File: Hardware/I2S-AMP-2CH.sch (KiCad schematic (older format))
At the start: 19 parts, among them U6 TAS5760MDCAR

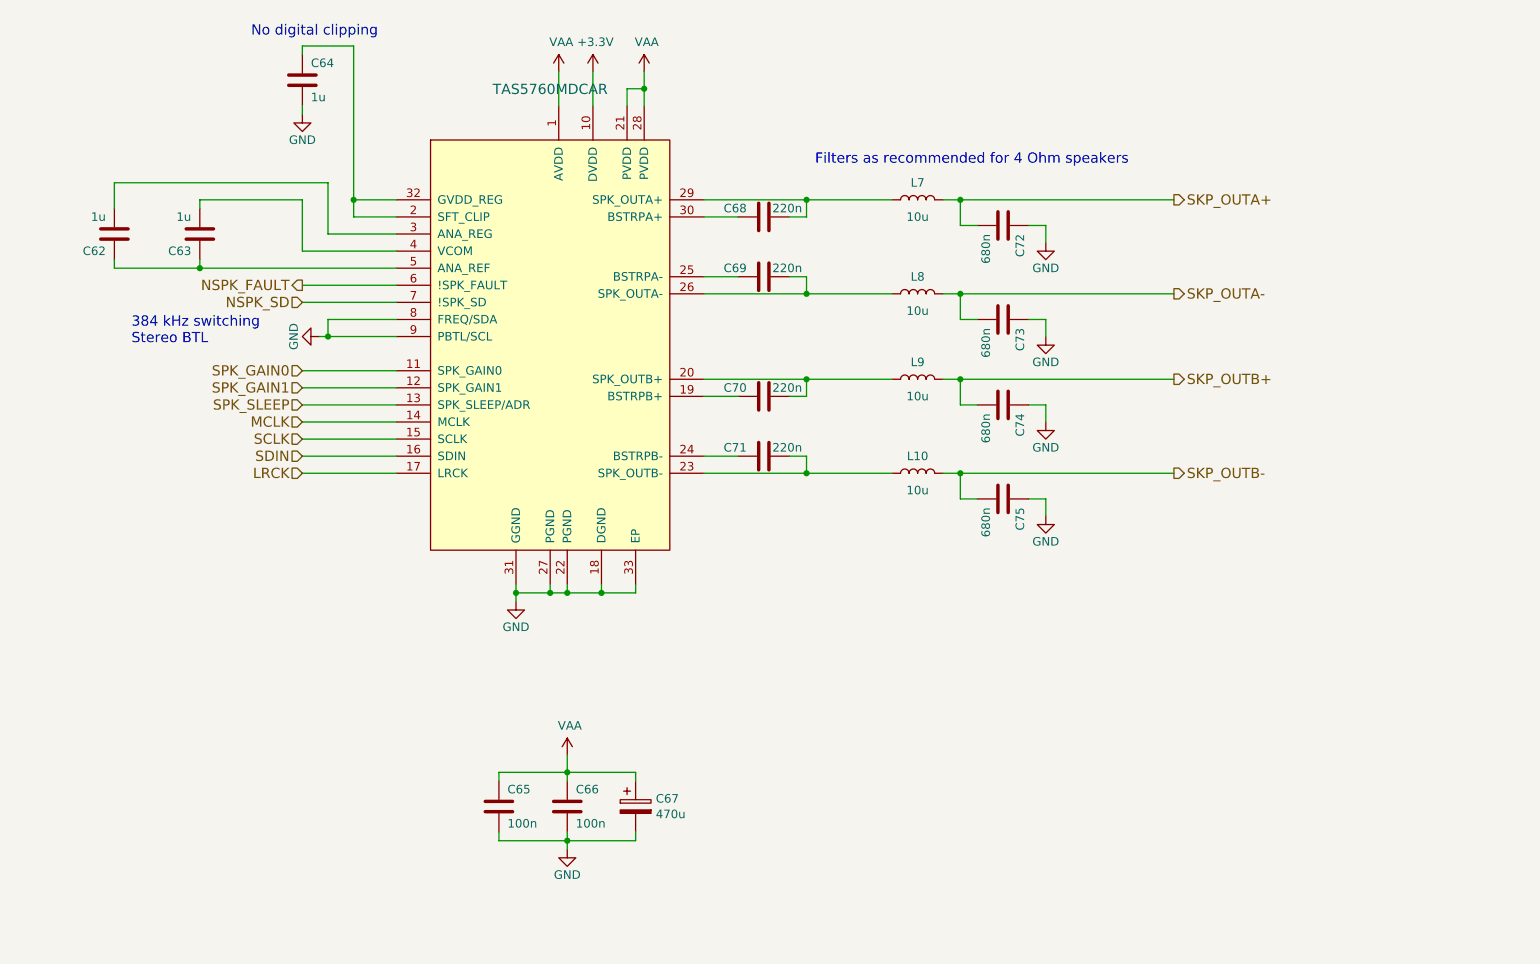
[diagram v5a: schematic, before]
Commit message: fixed usbi/ext header positions
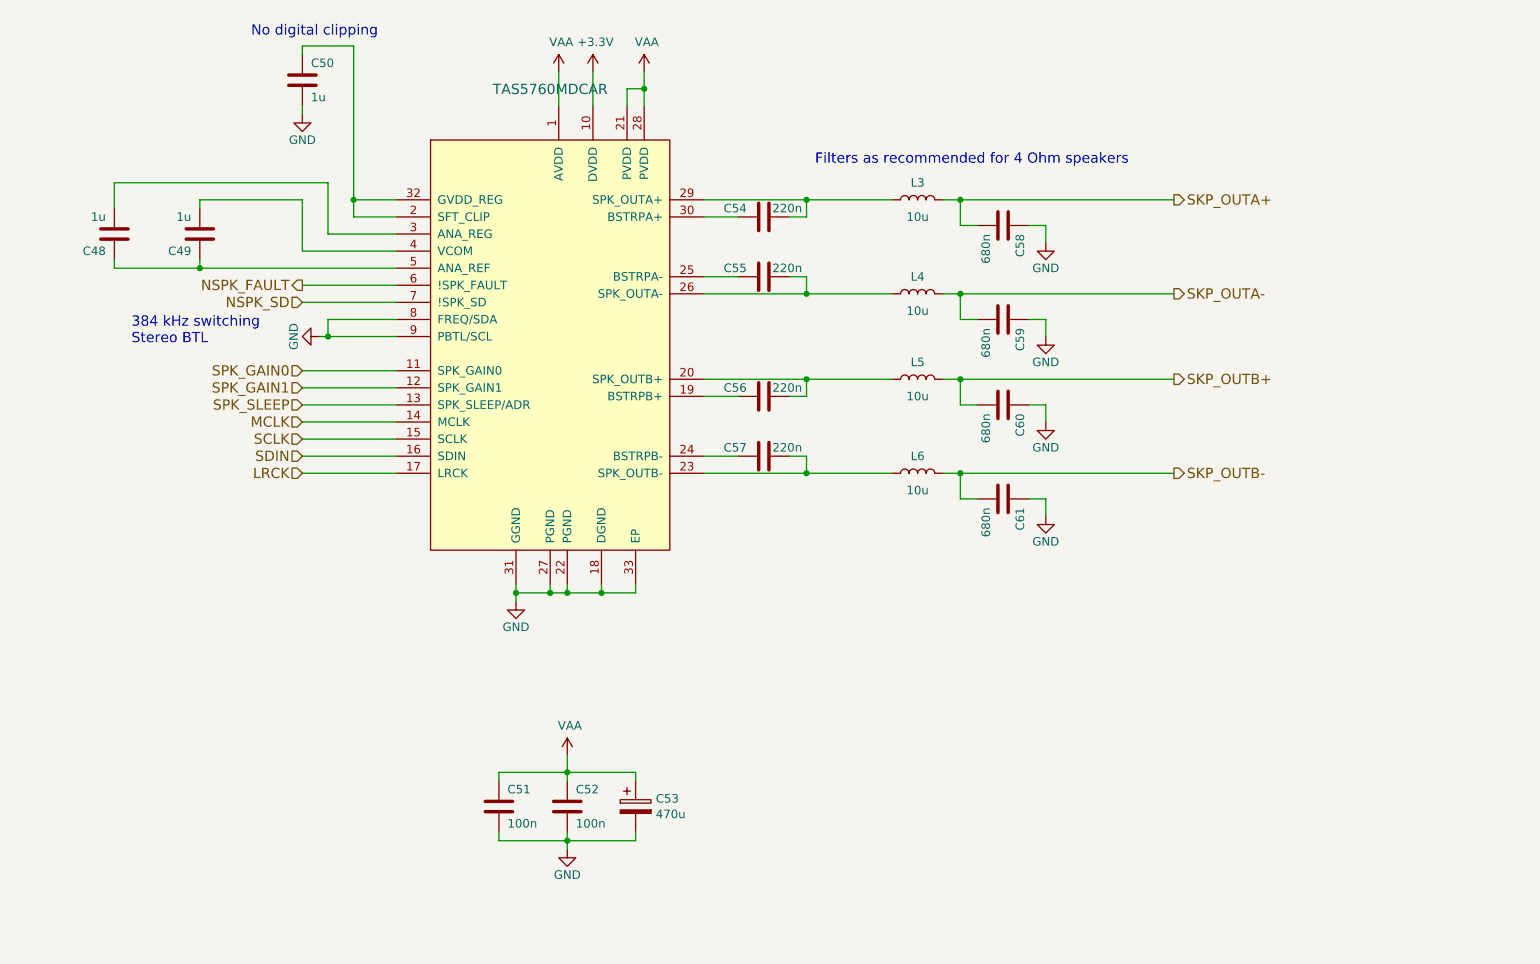
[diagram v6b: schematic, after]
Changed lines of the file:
@@
 AR Path="/5AF9FF80/574C11BE" Ref="C50"  Part="1"
 AR Path="/608A6138/574C11BE" Ref="C64"  Part="1"
-F 0 "C64" H 3000 1750 50  0000 L CNN
+F 0 "C50" H 3000 1750 50  0000 L CNN
 F 1 "1u" H 3000 1550 50  0000 L CNN
 F 2 "Capacitor_SMD:C_0805_2012Metric_Pad1.18x1.45mm_HandSolder" V 2650 1790 50  0001 C CNN
@@
 AR Path="/5AF9FF80/5B067CFE" Ref="C49"  Part="1"
 AR Path="/608A6138/5B067CFE" Ref="C63"  Part="1"
-F 0 "C63" H 2400 2650 50  0000 L CNN
+F 0 "C49" H 2400 2650 50  0000 L CNN
 F 1 "1u" H 2400 2450 50  0000 L CNN
 F 2 "Capacitor_SMD:C_0805_2012Metric_Pad1.18x1.45mm_HandSolder" V 2050 2690 50  0001 C CNN
@@
 AR Path="/5AF9FF80/5B067CFF" Ref="C48"  Part="1"
 AR Path="/608A6138/5B067CFF" Ref="C62"  Part="1"
-F 0 "C62" H 1900 2650 50  0000 L CNN
+F 0 "C48" H 1900 2650 50  0000 L CNN
 F 1 "1u" H 1900 2450 50  0000 L CNN
 F 2 "Capacitor_SMD:C_0805_2012Metric_Pad1.18x1.45mm_HandSolder" V 1550 2690 50  0001 C CNN
@@
 AR Path="/5AF9FF80/574C26C6" Ref="C52"  Part="1"
 AR Path="/608A6138/574C26C6" Ref="C66"  Part="1"
-F 0 "C66" H 4550 6000 50  0000 L CNN
+F 0 "C52" H 4550 6000 50  0000 L CNN
 F 1 "100n" H 4550 5800 50  0000 L CNN
 F 2 "Capacitor_SMD:C_0603_1608Metric_Pad1.08x0.95mm_HandSolder" V 4200 6040 50  0001 C CNN
@@
 AR Path="/5AF9FF80/5B067D07" Ref="#PWR078"  Part="1"
 AR Path="/608A6138/5B067D07" Ref="#PWR091"  Part="1"
-F 0 "#PWR091" H 4500 5900 50  0001 C CNN
+F 0 "#PWR078" H 4500 5900 50  0001 C CNN
 F 1 "GND" H 4500 6000 50  0000 C CNN
 F 2 "" H 4500 6150 50  0000 C CNN
@@
 AR Path="/5AF9FF80/5B067D09" Ref="#PWR072"  Part="1"
 AR Path="/608A6138/5B067D09" Ref="#PWR085"  Part="1"
-F 0 "#PWR085" H 2950 1600 50  0001 C CNN
+F 0 "#PWR072" H 2950 1600 50  0001 C CNN
 F 1 "GND" H 2950 1700 50  0000 C CNN
 F 2 "" H 2950 1850 50  0000 C CNN
@@
 AR Path="/5AF9FF80/5B067D0D" Ref="C57"  Part="1"
 AR Path="/608A6138/5B067D0D" Ref="C71"  Part="1"
-F 0 "C71" V 5700 3950 50  0000 L CNN
+F 0 "C57" V 5700 3950 50  0000 L CNN
 F 1 "220n" V 5700 3800 50  0000 R CNN
 F 2 "Capacitor_SMD:C_0603_1608Metric_Pad1.08x0.95mm_HandSolder" V 5350 3990 50  0001 C CNN
@@
 AR Path="/5AF9FF80/5B067D11" Ref="C55"  Part="1"
 AR Path="/608A6138/5B067D11" Ref="C69"  Part="1"
-F 0 "C69" V 5700 2900 50  0000 L CNN
+F 0 "C55" V 5700 2900 50  0000 L CNN
 F 1 "220n" V 5700 2750 50  0000 R CNN
 F 2 "Capacitor_SMD:C_0603_1608Metric_Pad1.08x0.95mm_HandSolder" V 5350 2940 50  0001 C CNN
@@
 AR Path="/5AF9FF80/5B067D13" Ref="C54"  Part="1"
 AR Path="/608A6138/5B067D13" Ref="C68"  Part="1"
-F 0 "C68" V 5700 2550 50  0000 L CNN
+F 0 "C54" V 5700 2550 50  0000 L CNN
 F 1 "220n" V 5700 2400 50  0000 R CNN
 F 2 "Capacitor_SMD:C_0603_1608Metric_Pad1.08x0.95mm_HandSolder" V 5350 2590 50  0001 C CNN
@@
 AR Path="/5AF9FF80/60755A7B" Ref="#PWR077"  Part="1"
 AR Path="/608A6138/60755A7B" Ref="#PWR090"  Part="1"
-F 0 "#PWR090" H 4500 5450 50  0001 C CNN
+F 0 "#PWR077" H 4500 5450 50  0001 C CNN
 F 1 "VAA" H 4515 5773 50  0000 C CNN
 F 2 "" H 4500 5600 50  0001 C CNN
@@
 AR Path="/5AF9FF80/60941DE7" Ref="#PWR079"  Part="1"
 AR Path="/608A6138/60941DE7" Ref="#PWR092"  Part="1"
-F 0 "#PWR092" H 4650 1450 50  0001 C CNN
+F 0 "#PWR079" H 4650 1450 50  0001 C CNN
 F 1 "+3.3V" H 4665 1773 50  0000 C CNN
 F 2 "" H 4650 1600 50  0001 C CNN
@@
 AR Path="/5AF9FF80/60945F7C" Ref="#PWR080"  Part="1"
 AR Path="/608A6138/60945F7C" Ref="#PWR093"  Part="1"
-F 0 "#PWR093" H 4950 1450 50  0001 C CNN
+F 0 "#PWR080" H 4950 1450 50  0001 C CNN
 F 1 "VAA" H 4965 1773 50  0000 C CNN
 F 2 "" H 4950 1600 50  0001 C CNN
@@
 AR Path="/5AF9FF80/60959421" Ref="#PWR076"  Part="1"
 AR Path="/608A6138/60959421" Ref="#PWR089"  Part="1"
-F 0 "#PWR089" H 4450 1450 50  0001 C CNN
+F 0 "#PWR076" H 4450 1450 50  0001 C CNN
 F 1 "VAA" H 4465 1773 50  0000 C CNN
 F 2 "" H 4450 1600 50  0001 C CNN
@@
 AR Path="/5AF9FF80/60963351" Ref="#PWR075"  Part="1"
 AR Path="/608A6138/60963351" Ref="#PWR088"  Part="1"
-F 0 "#PWR088" H 4200 4450 50  0001 C CNN
+F 0 "#PWR075" H 4200 4450 50  0001 C CNN
 F 1 "GND" H 4200 4550 50  0000 C CNN
 F 2 "" H 4200 4700 50  0000 C CNN
@@
 AR Path="/5AF9FF80/6097B2F1" Ref="C53"  Part="1"
 AR Path="/608A6138/6097B2F1" Ref="C67"  Part="1"
-F 0 "C67" H 5018 5946 50  0000 L CNN
+F 0 "C53" H 5018 5946 50  0000 L CNN
 F 1 "470u" H 5018 5855 50  0000 L CNN
 F 2 "Capacitor_THT:CP_Radial_D16.0mm_P7.50mm" H 4938 5750 50  0001 C CNN
@@
 AR Path="/5AF9FF80/60988667" Ref="C51"  Part="1"
 AR Path="/608A6138/60988667" Ref="C65"  Part="1"
-F 0 "C65" H 4150 6000 50  0000 L CNN
+F 0 "C51" H 4150 6000 50  0000 L CNN
 F 1 "100n" H 4150 5800 50  0000 L CNN
 F 2 "Capacitor_SMD:C_0603_1608Metric_Pad1.08x0.95mm_HandSolder" V 3800 6040 50  0001 C CNN
@@
 AR Path="/5AF9FF80/5B067D14" Ref="L3"  Part="1"
 AR Path="/608A6138/5B067D14" Ref="L7"  Part="1"
-F 0 "L7" V 6650 2350 50  0000 C CNN
+F 0 "L3" V 6650 2350 50  0000 C CNN
 F 1 "10u" V 6450 2350 50  0000 C CNN
 F 2 "Inductor_SMD:L_Abracon_ASPI-0630LR" H 6550 2350 50  0001 C CNN
@@
 AR Path="/5AF9FF80/60D816DE" Ref="L4"  Part="1"
 AR Path="/608A6138/60D816DE" Ref="L8"  Part="1"
-F 0 "L8" V 6650 2900 50  0000 C CNN
+F 0 "L4" V 6650 2900 50  0000 C CNN
 F 1 "10u" V 6450 2900 50  0000 C CNN
 F 2 "Inductor_SMD:L_Abracon_ASPI-0630LR" H 6550 2900 50  0001 C CNN
@@
 AR Path="/5AF9FF80/60D87D8D" Ref="L5"  Part="1"
 AR Path="/608A6138/60D87D8D" Ref="L9"  Part="1"
-F 0 "L9" V 6650 3400 50  0000 C CNN
+F 0 "L5" V 6650 3400 50  0000 C CNN
 F 1 "10u" V 6450 3400 50  0000 C CNN
 F 2 "Inductor_SMD:L_Abracon_ASPI-0630LR" H 6550 3400 50  0001 C CNN
@@
 AR Path="/5AF9FF80/60D87DA0" Ref="L6"  Part="1"
 AR Path="/608A6138/60D87DA0" Ref="L10"  Part="1"
-F 0 "L10" V 6650 3950 50  0000 C CNN
+F 0 "L6" V 6650 3950 50  0000 C CNN
 F 1 "10u" V 6450 3950 50  0000 C CNN
 F 2 "Inductor_SMD:L_Abracon_ASPI-0630LR" H 6550 3950 50  0001 C CNN
@@
 AR Path="/5AF9FF80/5B067D19" Ref="C58"  Part="1"
 AR Path="/608A6138/5B067D19" Ref="C72"  Part="1"
-F 0 "C72" H 7100 2600 50  0000 L CNN
+F 0 "C58" H 7100 2600 50  0000 L CNN
 F 1 "680n" H 7100 2400 50  0000 L CNN
 F 2 "Capacitor_SMD:C_0603_1608Metric_Pad1.08x0.95mm_HandSolder" V 6750 2640 50  0001 C CNN
@@
 AR Path="/5AF9FF80/60D9BA43" Ref="C59"  Part="1"
 AR Path="/608A6138/60D9BA43" Ref="C73"  Part="1"
-F 0 "C73" H 7100 3150 50  0000 L CNN
+F 0 "C59" H 7100 3150 50  0000 L CNN
 F 1 "680n" H 7100 2950 50  0000 L CNN
 F 2 "Capacitor_SMD:C_0603_1608Metric_Pad1.08x0.95mm_HandSolder" V 6750 3190 50  0001 C CNN
@@
 AR Path="/5AF9FF80/60D9DAD3" Ref="C60"  Part="1"
 AR Path="/608A6138/60D9DAD3" Ref="C74"  Part="1"
-F 0 "C74" H 7100 3650 50  0000 L CNN
+F 0 "C60" H 7100 3650 50  0000 L CNN
 F 1 "680n" H 7100 3450 50  0000 L CNN
 F 2 "Capacitor_SMD:C_0603_1608Metric_Pad1.08x0.95mm_HandSolder" V 6750 3690 50  0001 C CNN
@@
 AR Path="/5AF9FF80/60D9FB44" Ref="C61"  Part="1"
 AR Path="/608A6138/60D9FB44" Ref="C75"  Part="1"
-F 0 "C75" H 7100 4200 50  0000 L CNN
+F 0 "C61" H 7100 4200 50  0000 L CNN
 F 1 "680n" H 7100 4000 50  0000 L CNN
 F 2 "Capacitor_SMD:C_0603_1608Metric_Pad1.08x0.95mm_HandSolder" V 6750 4240 50  0001 C CNN
@@
 AR Path="/5AF9FF80/60DA7B3F" Ref="#PWR081"  Part="1"
 AR Path="/608A6138/60DA7B3F" Ref="#PWR094"  Part="1"
-F 0 "#PWR094" H 7300 2350 50  0001 C CNN
+F 0 "#PWR081" H 7300 2350 50  0001 C CNN
 F 1 "GND" H 7300 2450 50  0000 C CNN
 F 2 "" H 7300 2600 50  0000 C CNN
@@
 AR Path="/5AF9FF80/60DA836C" Ref="#PWR082"  Part="1"
 AR Path="/608A6138/60DA836C" Ref="#PWR095"  Part="1"
-F 0 "#PWR095" H 7300 2900 50  0001 C CNN
+F 0 "#PWR082" H 7300 2900 50  0001 C CNN
 F 1 "GND" H 7300 3000 50  0000 C CNN
 F 2 "" H 7300 3150 50  0000 C CNN
@@
 AR Path="/5AF9FF80/60DA880A" Ref="#PWR083"  Part="1"
 AR Path="/608A6138/60DA880A" Ref="#PWR096"  Part="1"
-F 0 "#PWR096" H 7300 3400 50  0001 C CNN
+F 0 "#PWR083" H 7300 3400 50  0001 C CNN
 F 1 "GND" H 7300 3500 50  0000 C CNN
 F 2 "" H 7300 3650 50  0000 C CNN
@@
 AR Path="/5AF9FF80/60DA8B92" Ref="#PWR084"  Part="1"
 AR Path="/608A6138/60DA8B92" Ref="#PWR097"  Part="1"
-F 0 "#PWR097" H 7300 3950 50  0001 C CNN
+F 0 "#PWR084" H 7300 3950 50  0001 C CNN
 F 1 "GND" H 7300 4050 50  0000 C CNN
 F 2 "" H 7300 4200 50  0000 C CNN
@@
 AR Path="/5AF9FF80/60C136E8" Ref="C56"  Part="1"
 AR Path="/608A6138/60C136E8" Ref="C70"  Part="1"
-F 0 "C70" V 5700 3600 50  0000 L CNN
+F 0 "C56" V 5700 3600 50  0000 L CNN
 F 1 "220n" V 5700 3450 50  0000 R CNN
 F 2 "Capacitor_SMD:C_0603_1608Metric_Pad1.08x0.95mm_HandSolder" V 5350 3640 50  0001 C CNN
@@
 AR Path="/5AF9FF80/60B105F1" Ref="#PWR0122"  Part="1"
 AR Path="/608A6138/60B105F1" Ref="#PWR0124"  Part="1"
-F 0 "#PWR0124" H 3050 2900 50  0001 C CNN
+F 0 "#PWR0122" H 3050 2900 50  0001 C CNN
 F 1 "GND" H 3050 3000 50  0000 C CNN
 F 2 "" H 3050 3150 50  0000 C CNN
@@
 AR Path="/5AF9FF80/608A7BF7" Ref="U6"  Part="1"
 AR Path="/608A6138/608A7BF7" Ref="U7"  Part="1"
-F 0 "U7" H 4400 5150 60  0001 C TNN
+F 0 "U6" H 4400 5150 60  0001 C TNN
 F 1 "TAS5760MDCAR" H 4400 4697 60  0000 C CNN
 F 2 "Package_SO:HTSSOP-32-1EP_6.1x11mm_P0.65mm_EP5.2x11mm_Mask4.11x4.36mm_ThermalVias" H 4300 3100 60  0001 C CNN

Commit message: hardware bugfixes
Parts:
- C58, C59, C60, C61: footprint Capacitor_SMD:C_0603_1608Metric_Pad1.08x0.95mm_HandSolder -> Capacitor_SMD:C_0805_2012Metric_Pad1.18x1.45mm_HandSolder
- renumbered U6 to U7

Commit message: various bugfixes
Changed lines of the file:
@@
 $Descr A4 11693 8268
 encoding utf-8
-Sheet 5 8
+Sheet 4 8
 Title "AMP"
 Date "2021-03-30"
@@
 AR Path="/5AF9FF80/574C11BE" Ref="C50"  Part="1"
 AR Path="/608A6138/574C11BE" Ref="C64"  Part="1"
-F 0 "C64" H 3000 1750 50  0000 L CNN
+F 0 "C50" H 3000 1750 50  0000 L CNN
 F 1 "1u" H 3000 1550 50  0000 L CNN
 F 2 "Capacitor_SMD:C_0805_2012Metric_Pad1.18x1.45mm_HandSolder" V 2650 1790 50  0001 C CNN
@@
 AR Path="/5AF9FF80/5B067CFE" Ref="C49"  Part="1"
 AR Path="/608A6138/5B067CFE" Ref="C63"  Part="1"
-F 0 "C63" H 2400 2650 50  0000 L CNN
+F 0 "C49" H 2400 2650 50  0000 L CNN
 F 1 "1u" H 2400 2450 50  0000 L CNN
 F 2 "Capacitor_SMD:C_0805_2012Metric_Pad1.18x1.45mm_HandSolder" V 2050 2690 50  0001 C CNN
@@
 AR Path="/5AF9FF80/5B067CFF" Ref="C48"  Part="1"
 AR Path="/608A6138/5B067CFF" Ref="C62"  Part="1"
-F 0 "C62" H 1900 2650 50  0000 L CNN
+F 0 "C48" H 1900 2650 50  0000 L CNN
 F 1 "1u" H 1900 2450 50  0000 L CNN
 F 2 "Capacitor_SMD:C_0805_2012Metric_Pad1.18x1.45mm_HandSolder" V 1550 2690 50  0001 C CNN
@@
 AR Path="/5AF9FF80/574C26C6" Ref="C52"  Part="1"
 AR Path="/608A6138/574C26C6" Ref="C66"  Part="1"
-F 0 "C66" H 4550 6000 50  0000 L CNN
+F 0 "C52" H 4550 6000 50  0000 L CNN
 F 1 "100n" H 4550 5800 50  0000 L CNN
 F 2 "Capacitor_SMD:C_0603_1608Metric_Pad1.08x0.95mm_HandSolder" V 4200 6040 50  0001 C CNN
@@
 AR Path="/5AF9FF80/5B067D0D" Ref="C57"  Part="1"
 AR Path="/608A6138/5B067D0D" Ref="C71"  Part="1"
-F 0 "C71" V 5700 3950 50  0000 L CNN
+F 0 "C57" V 5700 3950 50  0000 L CNN
 F 1 "220n" V 5700 3800 50  0000 R CNN
 F 2 "Capacitor_SMD:C_0603_1608Metric_Pad1.08x0.95mm_HandSolder" V 5350 3990 50  0001 C CNN
@@
 AR Path="/5AF9FF80/5B067D11" Ref="C55"  Part="1"
 AR Path="/608A6138/5B067D11" Ref="C69"  Part="1"
-F 0 "C69" V 5700 2900 50  0000 L CNN
+F 0 "C55" V 5700 2900 50  0000 L CNN
 F 1 "220n" V 5700 2750 50  0000 R CNN
 F 2 "Capacitor_SMD:C_0603_1608Metric_Pad1.08x0.95mm_HandSolder" V 5350 2940 50  0001 C CNN
@@
 AR Path="/5AF9FF80/5B067D13" Ref="C54"  Part="1"
 AR Path="/608A6138/5B067D13" Ref="C68"  Part="1"
-F 0 "C68" V 5700 2550 50  0000 L CNN
+F 0 "C54" V 5700 2550 50  0000 L CNN
 F 1 "220n" V 5700 2400 50  0000 R CNN
 F 2 "Capacitor_SMD:C_0603_1608Metric_Pad1.08x0.95mm_HandSolder" V 5350 2590 50  0001 C CNN
@@
 AR Path="/5AF9FF80/6097B2F1" Ref="C53"  Part="1"
 AR Path="/608A6138/6097B2F1" Ref="C67"  Part="1"
-F 0 "C67" H 5018 5946 50  0000 L CNN
+F 0 "C53" H 5018 5946 50  0000 L CNN
 F 1 "470u" H 5018 5855 50  0000 L CNN
 F 2 "Capacitor_THT:CP_Radial_D16.0mm_P7.50mm" H 4938 5750 50  0001 C CNN
@@
 AR Path="/5AF9FF80/60988667" Ref="C51"  Part="1"
 AR Path="/608A6138/60988667" Ref="C65"  Part="1"
-F 0 "C65" H 4150 6000 50  0000 L CNN
+F 0 "C51" H 4150 6000 50  0000 L CNN
 F 1 "100n" H 4150 5800 50  0000 L CNN
 F 2 "Capacitor_SMD:C_0603_1608Metric_Pad1.08x0.95mm_HandSolder" V 3800 6040 50  0001 C CNN
@@
 AR Path="/5AF9FF80/5B067D14" Ref="L3"  Part="1"
 AR Path="/608A6138/5B067D14" Ref="L7"  Part="1"
-F 0 "L7" V 6650 2350 50  0000 C CNN
+F 0 "L3" V 6650 2350 50  0000 C CNN
 F 1 "10u" V 6450 2350 50  0000 C CNN
 F 2 "Inductor_SMD:L_Abracon_ASPI-0630LR" H 6550 2350 50  0001 C CNN
@@
 AR Path="/5AF9FF80/60D816DE" Ref="L4"  Part="1"
 AR Path="/608A6138/60D816DE" Ref="L8"  Part="1"
-F 0 "L8" V 6650 2900 50  0000 C CNN
+F 0 "L4" V 6650 2900 50  0000 C CNN
 F 1 "10u" V 6450 2900 50  0000 C CNN
 F 2 "Inductor_SMD:L_Abracon_ASPI-0630LR" H 6550 2900 50  0001 C CNN
@@
 AR Path="/5AF9FF80/60D87D8D" Ref="L5"  Part="1"
 AR Path="/608A6138/60D87D8D" Ref="L9"  Part="1"
-F 0 "L9" V 6650 3400 50  0000 C CNN
+F 0 "L5" V 6650 3400 50  0000 C CNN
 F 1 "10u" V 6450 3400 50  0000 C CNN
 F 2 "Inductor_SMD:L_Abracon_ASPI-0630LR" H 6550 3400 50  0001 C CNN
@@
 AR Path="/5AF9FF80/60D87DA0" Ref="L6"  Part="1"
 AR Path="/608A6138/60D87DA0" Ref="L10"  Part="1"
-F 0 "L10" V 6650 3950 50  0000 C CNN
+F 0 "L6" V 6650 3950 50  0000 C CNN
 F 1 "10u" V 6450 3950 50  0000 C CNN
 F 2 "Inductor_SMD:L_Abracon_ASPI-0630LR" H 6550 3950 50  0001 C CNN
@@
 AR Path="/5AF9FF80/5B067D19" Ref="C58"  Part="1"
 AR Path="/608A6138/5B067D19" Ref="C72"  Part="1"
-F 0 "C72" H 7100 2600 50  0000 L CNN
+F 0 "C58" H 7100 2600 50  0000 L CNN
 F 1 "680n" H 7100 2400 50  0000 L CNN
 F 2 "Capacitor_SMD:C_0805_2012Metric_Pad1.18x1.45mm_HandSolder" V 6750 2640 50  0001 C CNN
@@
 AR Path="/5AF9FF80/60D9BA43" Ref="C59"  Part="1"
 AR Path="/608A6138/60D9BA43" Ref="C73"  Part="1"
-F 0 "C73" H 7100 3150 50  0000 L CNN
+F 0 "C59" H 7100 3150 50  0000 L CNN
 F 1 "680n" H 7100 2950 50  0000 L CNN
 F 2 "Capacitor_SMD:C_0805_2012Metric_Pad1.18x1.45mm_HandSolder" V 6750 3190 50  0001 C CNN
@@
 AR Path="/5AF9FF80/60D9DAD3" Ref="C60"  Part="1"
 AR Path="/608A6138/60D9DAD3" Ref="C74"  Part="1"
-F 0 "C74" H 7100 3650 50  0000 L CNN
+F 0 "C60" H 7100 3650 50  0000 L CNN
 F 1 "680n" H 7100 3450 50  0000 L CNN
 F 2 "Capacitor_SMD:C_0805_2012Metric_Pad1.18x1.45mm_HandSolder" V 6750 3690 50  0001 C CNN
@@
 AR Path="/5AF9FF80/60D9FB44" Ref="C61"  Part="1"
 AR Path="/608A6138/60D9FB44" Ref="C75"  Part="1"
-F 0 "C75" H 7100 4200 50  0000 L CNN
+F 0 "C61" H 7100 4200 50  0000 L CNN
 F 1 "680n" H 7100 4000 50  0000 L CNN
 F 2 "Capacitor_SMD:C_0805_2012Metric_Pad1.18x1.45mm_HandSolder" V 6750 4240 50  0001 C CNN
@@
 AR Path="/5AF9FF80/60C136E8" Ref="C56"  Part="1"
 AR Path="/608A6138/60C136E8" Ref="C70"  Part="1"
-F 0 "C70" V 5700 3600 50  0000 L CNN
+F 0 "C56" V 5700 3600 50  0000 L CNN
 F 1 "220n" V 5700 3450 50  0000 R CNN
 F 2 "Capacitor_SMD:C_0603_1608Metric_Pad1.08x0.95mm_HandSolder" V 5350 3640 50  0001 C CNN
@@
 AR Path="/5AF9FF80/608A7BF7" Ref="U7"  Part="1"
 AR Path="/608A6138/608A7BF7" Ref="U8"  Part="1"
-F 0 "U8" H 4400 5150 60  0001 C TNN
+F 0 "U7" H 4400 5150 60  0001 C TNN
 F 1 "TAS5760MDCAR" H 4400 4697 60  0000 C CNN
 F 2 "Package_SO:HTSSOP-32-1EP_6.1x11mm_P0.65mm_EP5.2x11mm_Mask4.11x4.36mm_ThermalVias" H 4300 3100 60  0001 C CNN
